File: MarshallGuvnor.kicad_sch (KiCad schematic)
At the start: 50 parts, among them J1 POWER, J2 INPUT, J3 OUTPUT, Q1 IRFD9120 PMOS, U1 TL084

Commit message: Minor bugfixes
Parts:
- D1: value D_Zener -> ~6.8V Zener
- R2: value 470 -> 2k2
- R3: value 100 -> 4k7
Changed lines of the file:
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@@
       (effects (font (size 1.27 1.27)) (justify left))
     )
-    (property "Value" "D_Zener" (at 73.66 36.83 90)
+    (property "Value" "~6.8V Zener" (at 73.66 36.83 90)
       (effects (font (size 1.27 1.27)) (justify left))
     )
@@
       (effects (font (size 1.27 1.27)) (justify right))
     )
-    (property "Value" "470" (at 119.38 46.99 0)
+    (property "Value" "2k2" (at 119.38 46.99 0)
       (effects (font (size 1.27 1.27)) (justify right))
     )
@@
       (effects (font (size 1.27 1.27)) (justify right))
     )
-    (property "Value" "100" (at 60.96 48.26 0)
-      (effects (font (size 1.27 1.27)) (justify right))
-    )
+    (property "Value" "4k7" (at 60.96 48.26 0)
+      (effects (font (size 1.27 1.27)) (justify right))
+    )

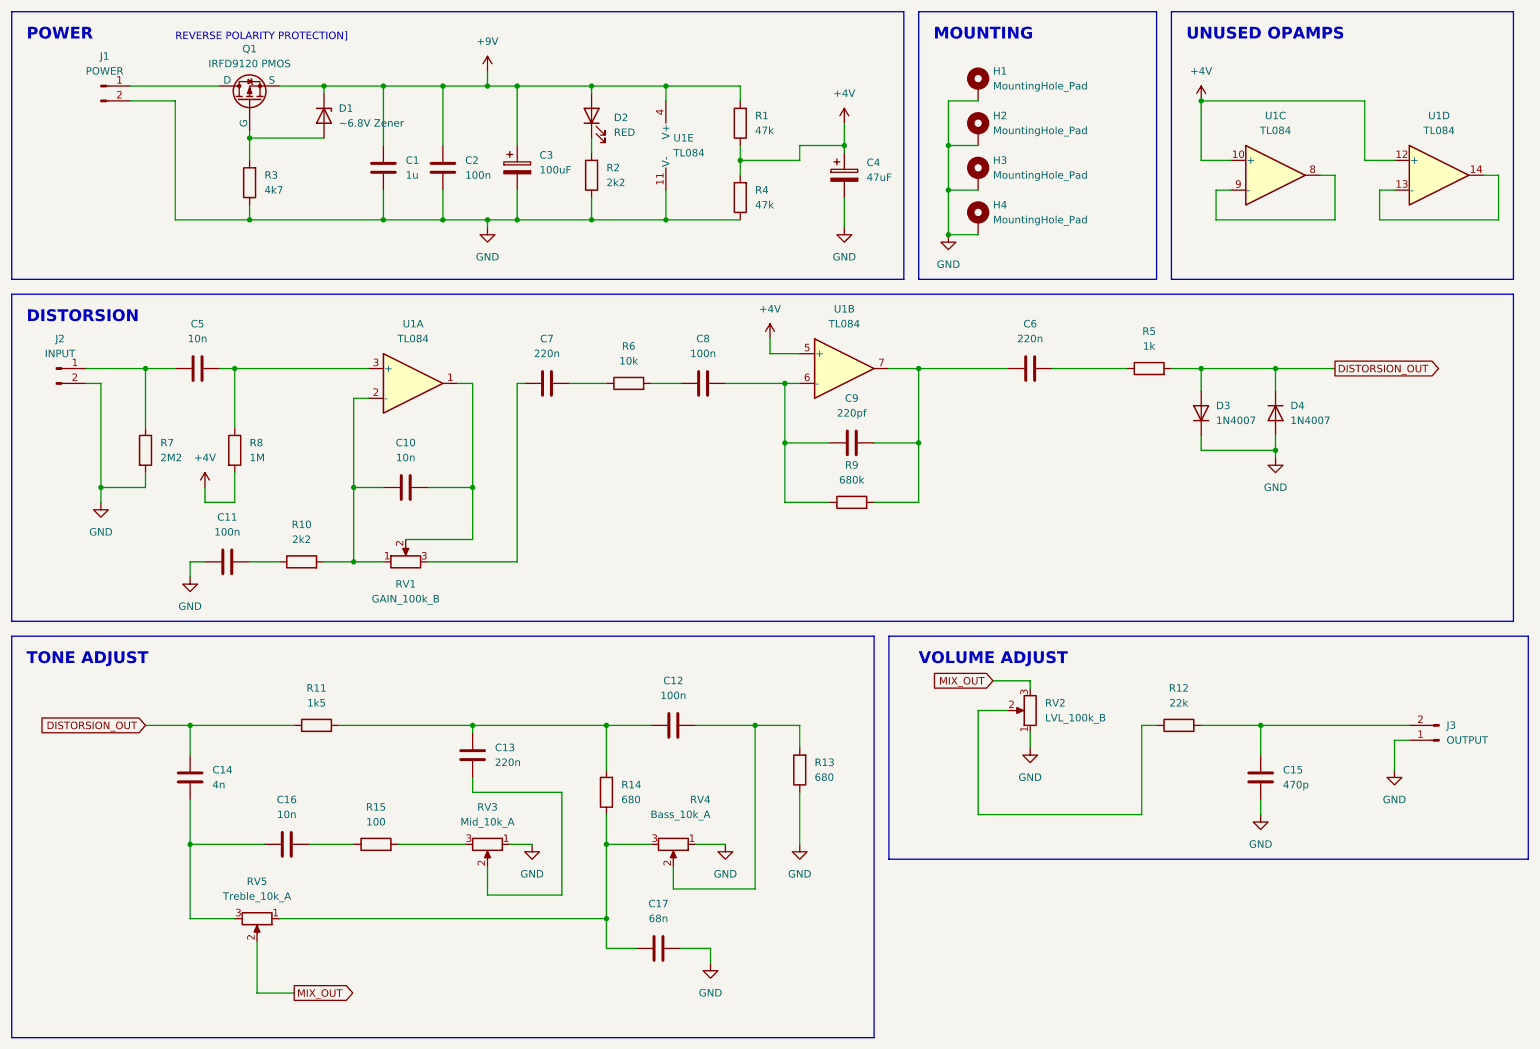
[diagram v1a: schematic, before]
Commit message: Update shcm, change one cap value, add footswitch
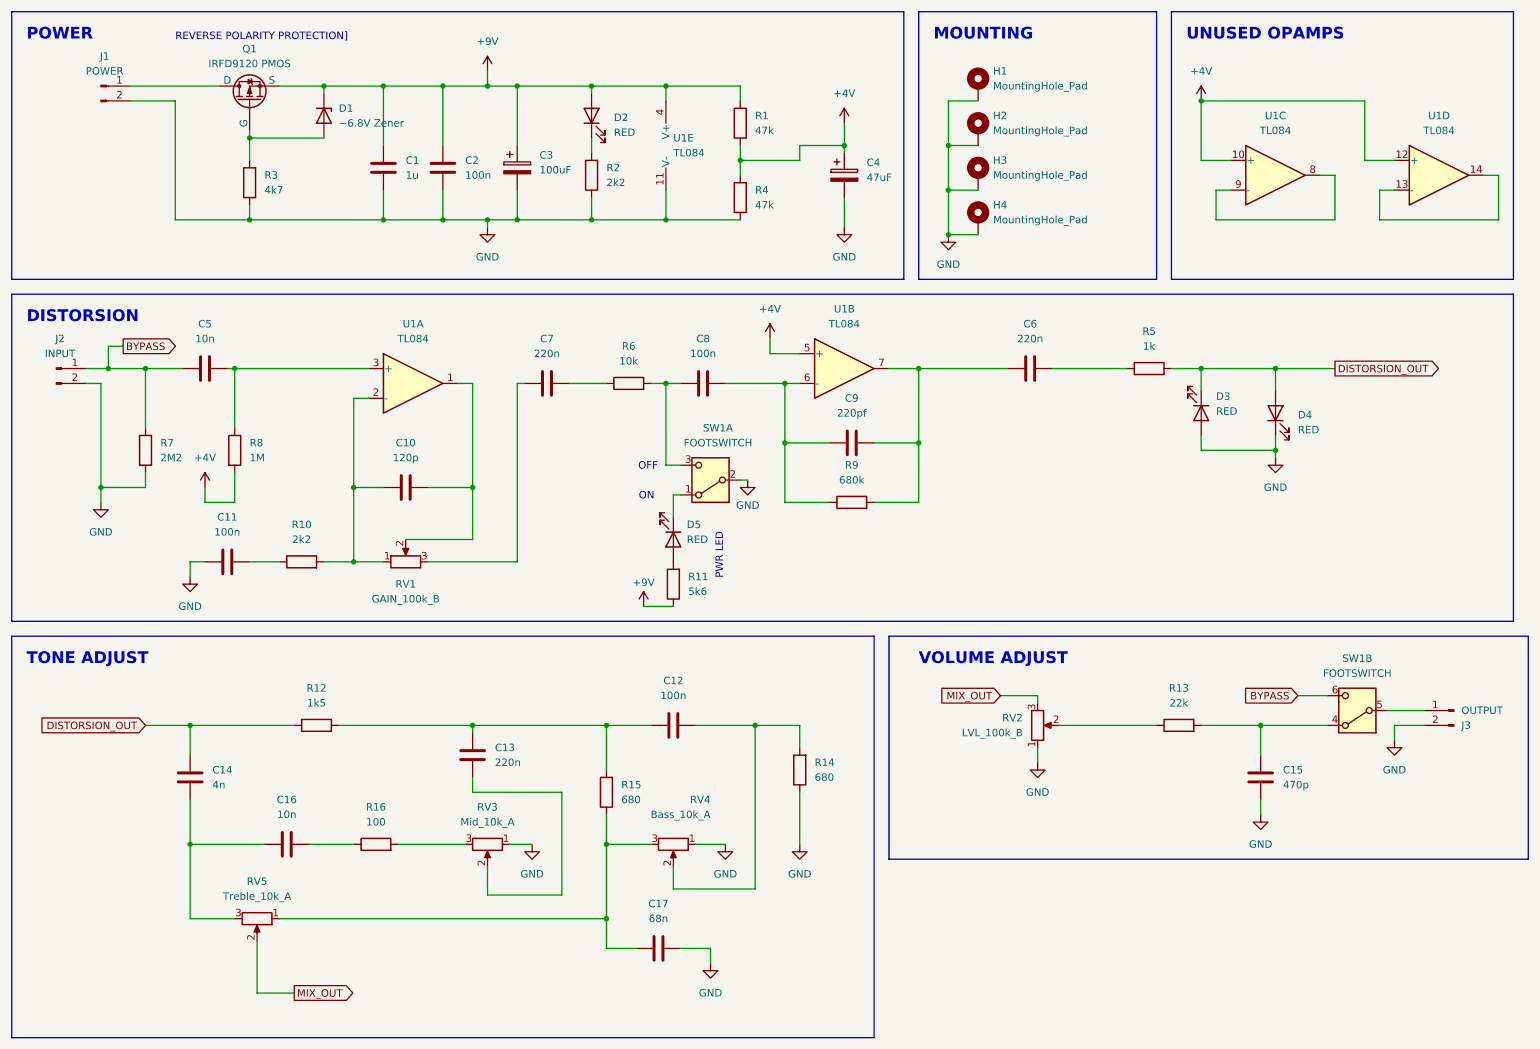
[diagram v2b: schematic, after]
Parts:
- removed D3, D4: 1N4007, Diode_THT:D_A-405_P7.62mm_Horizontal, symbol Device:D
- added D3, D4, D5: RED, LED_THT:LED_D5.0mm, symbol Device:LED
- added R11: 5k6, Resistor_SMD:R_1206_3216Metric, symbol Device:R
- added SW1: FOOTSWITCH, symbol Switch:SW_DPDT_x2
- C10: value 10n -> 120p
- D2: footprint LED_THT:LED_D5.0mm_FlatTop -> LED_THT:LED_D5.0mm
- renumbered R11 to R12, R12 to R13, R13 to R14, R14 to R15, R15 to R16
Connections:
- net +9V: now also R11.1
- net DISTORSION_OUT: now also D3.1 (K), D4.2 (A)
- net GND: now also J3.2 (Pin_2), D3.2 (A), D4.1 (K), SW1.2 (B); no longer J3.1 (Pin_1)
- net BYPASS: now reaches C5.1, J2.1 (Pin_1), R7.1
- net BYPASS: now also SW1.6 (C)
- net at C8.1, R6.2: now also SW1.3 (C)
- net at C15.2, R13.2: now also SW1.4 (A); no longer J3.2 (Pin_2)
- new net: D5.1 (K), SW1.1 (A)
- new net: J3.1 (Pin_1), SW1.5 (B)
- new net: D5.2 (A), R11.2
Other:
- note added: "OFF"
- note added: "ON"
- note added: "PWR LED"
- moved on the sheet: C5, J3, RV2
